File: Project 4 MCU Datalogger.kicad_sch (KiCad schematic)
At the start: 0 parts

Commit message: Setup of EEschema of new project.
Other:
- company: (none) -> Mad Tech T
- title: (none) -> ${project_name}
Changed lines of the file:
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@@
 	(generator_version "9.0")
 	(paper "A4")
+	(title_block
+		(title "${project_name}")
+		(date "2025-11-02")
+		(rev "1")
+		(company "Mad Tech T")
+	)
 	(sheet_instances
 		(path "/"

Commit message: Added required symbols to the schematic sheet.
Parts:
- added BT1: Battery, symbol Device:Battery
- added C1, C2, C4, C5: C, symbol Device:C
- added C3: C_Polarized, symbol Device:C_Polarized
- added D1, D2: LED, symbol Device:LED
- added H1, H2, H3, H4: MountingHole, symbol Mechanical:MountingHole
- added R1, R2, R3, R4, R5, R6, R7: R, symbol Device:R
- added U1, U2: 24LC1025, symbol Memory_EEPROM:24LC1025
- added U3: DS1337S_, DS1337S_:SOIC127P600X175-8N, symbol DS1337S_:DS1337S_
- added U4: ATMEGA328P-AU, ATMEGA328P-AU:QFP80P900X900X120-32N, symbol ATMEGA328P-AU:ATMEGA328P-AU
- added Y1, Y2: Crystal, symbol Device:Crystal
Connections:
- new net: U3.1 (X1), Y1.2
- new net: U3.2 (X2), Y1.1
- new net: R5.2, U3.3 (~{INTA})
- new net: R6.2, U3.7 (SQW/~INT)
- new net: C5.1, R5.1, R6.1, U3.8 (VCC)
- new net: D1.1 (K), R4.2
- new net: D1.2 (A), U4.17 (PB5)
- new net: BT1.1 (+), C3.1, D2.2 (A), U4.18 (AVCC)
- new net: D2.1 (K), R1.1
- new net: R2.1, R3.1
- new net: C1.2, U4.7 (PB6), Y2.2
- new net: R7.2, U4.29 (PC6/~{RESET})
- new net: C2.2, U4.8 (PB7), Y2.1
- new net: C4.2, U4.12 (PB0)
- new net: U4.21 (GND), U4.3 (GND), U4.5 (GND)
- new net: U4.4 (VCC), U4.6 (VCC)
- new net GND: BT1.2 (-), C1.1, C2.1, C3.2, C4.1, C5.2, R1.2, R4.1, U1.4 (GND), U1.7 (WP), U2.2 (A1), U2.4 (GND), U2.7 (WP), U3.4 (GND)
- no-connect marks 0 -> 8
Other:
- added sheet Connectors (connectors.kicad_sch)

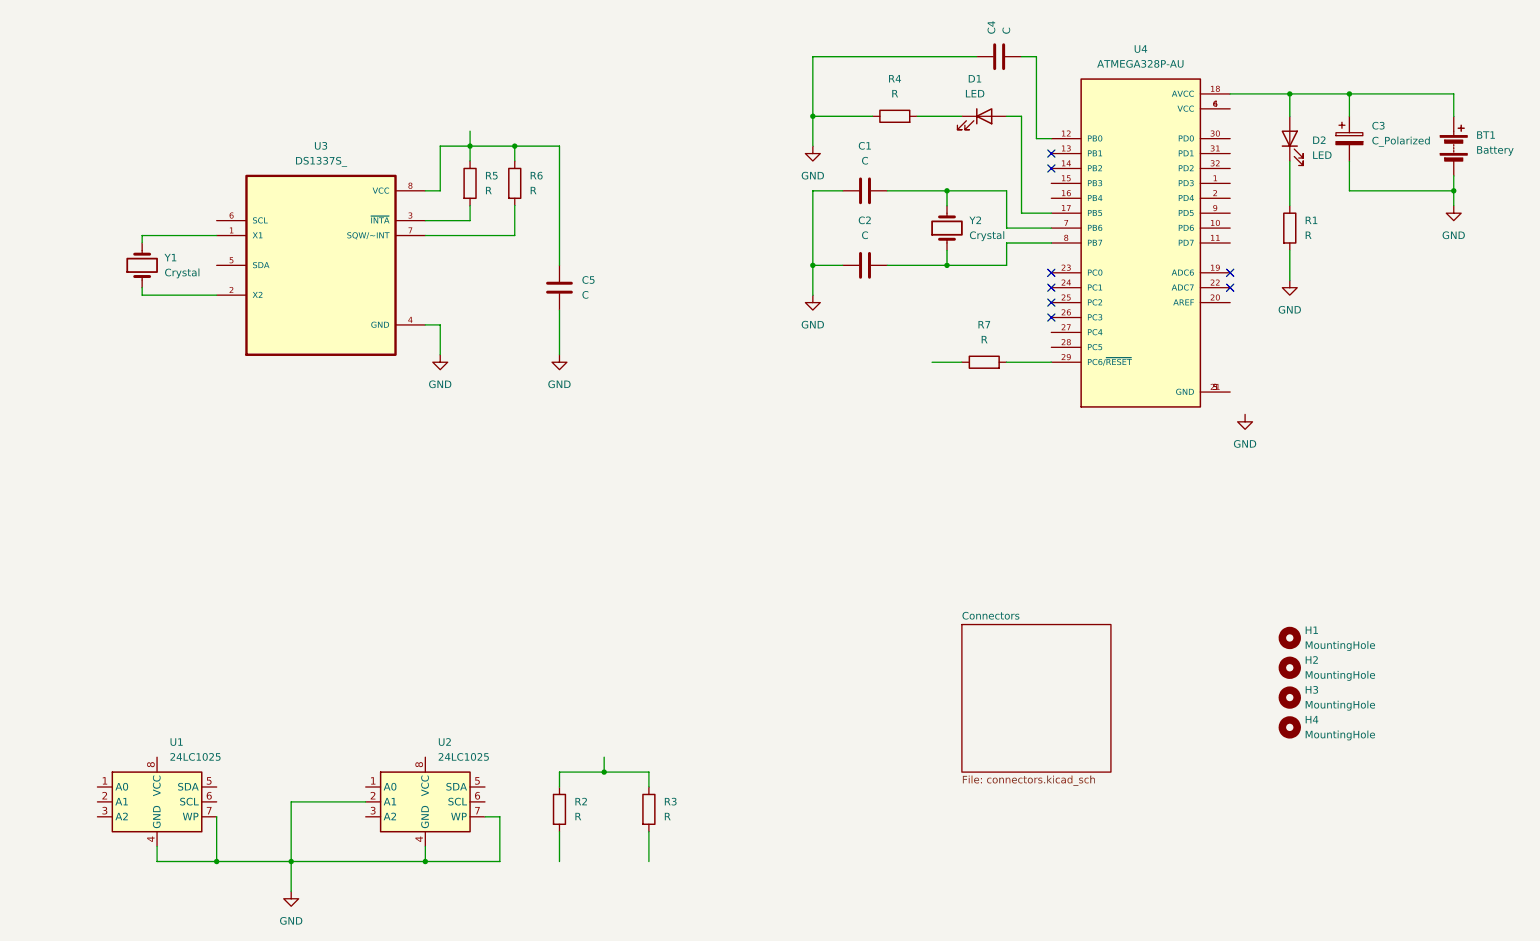
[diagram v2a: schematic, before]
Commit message: completed symbol-footprint association.
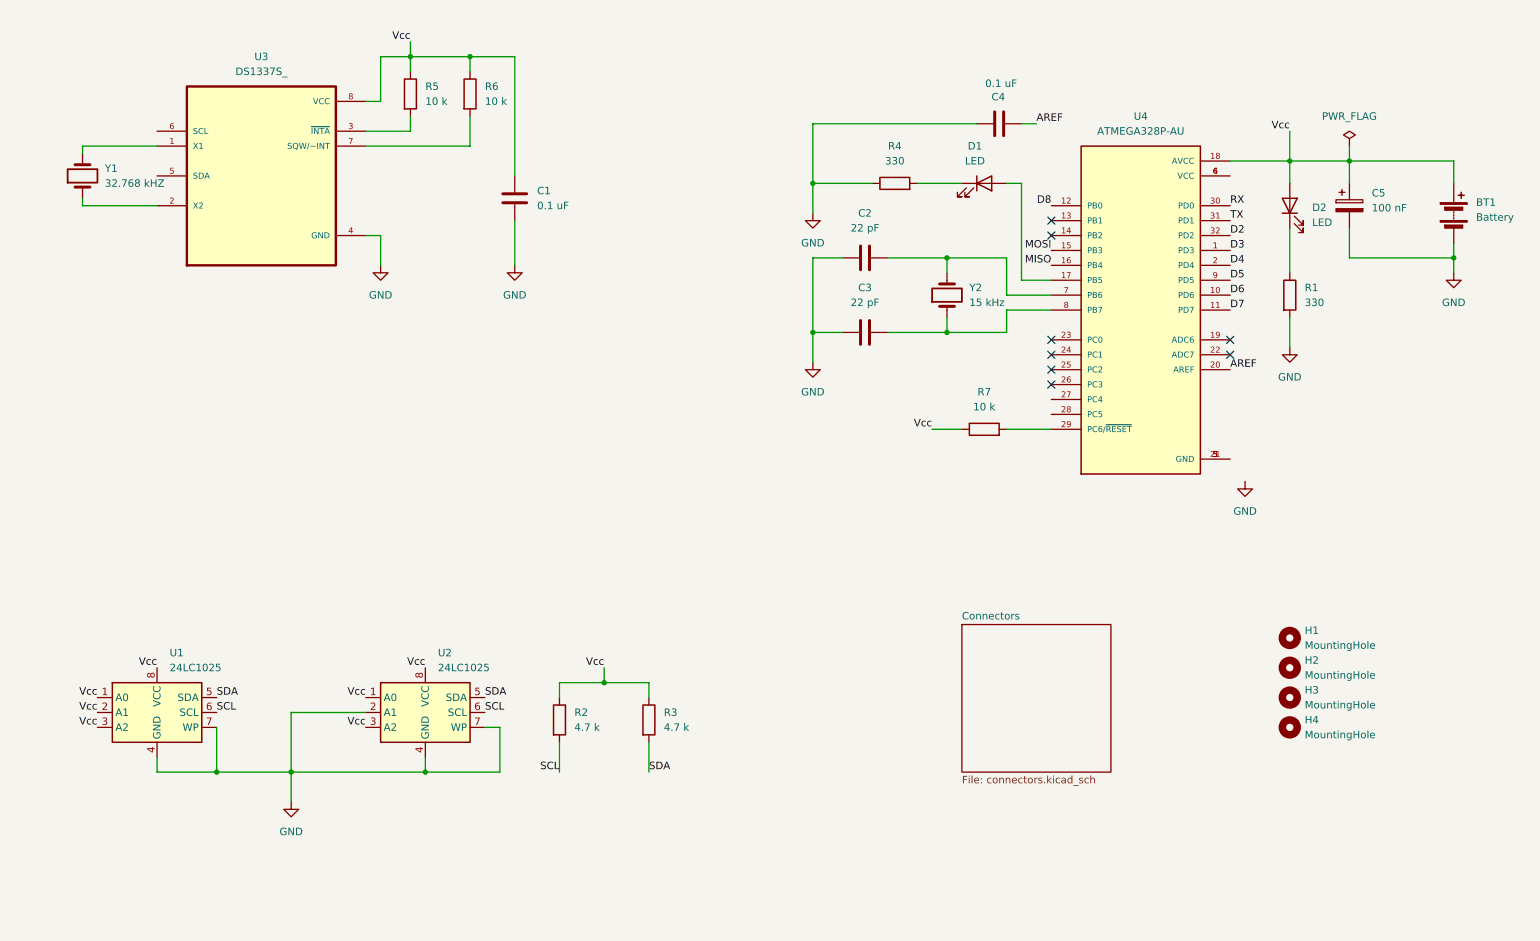
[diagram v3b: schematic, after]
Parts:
- BT1: footprint (none) -> Connector_PinHeader_2.54mm:PinHeader_1x02_P2.54mm_Vertical
- C1: renamed from C5; value C -> 0.1 uF; footprint (none) -> Capacitor_SMD:C_0805_2012Metric
- C2: renamed from C1; value C -> 22 pF; footprint (none) -> Capacitor_SMD:C_0805_2012Metric
- C3: renamed from C2; value C -> 22 pF; footprint (none) -> Capacitor_SMD:C_0805_2012Metric
- C4: value C -> 0.1 uF; footprint (none) -> Capacitor_SMD:C_0805_2012Metric
- C5: renamed from C3; value C_Polarized -> 100 nF; footprint (none) -> Capacitor_SMD:C_0805_2012Metric
- D1, D2: footprint (none) -> LED_SMD:LED_0805_2012Metric
- H1, H2, H3, H4: footprint (none) -> MountingHole:MountingHole_2.1mm
- R1, R4: value R -> 330; footprint (none) -> Resistor_SMD:R_0805_2012Metric
- R2, R3: value R -> 4.7 k; footprint (none) -> Resistor_SMD:R_0805_2012Metric
- R5, R6, R7: value R -> 10 k; footprint (none) -> Resistor_SMD:R_0805_2012Metric
- U1, U2: footprint (none) -> Package_SO:SOIC-8_5.3x5.3mm_P1.27mm
- U3: footprint DS1337S_:SOIC127P600X175-8N -> MCU_Datalogger_Footprints:SOIC127P600X175-8N
- U4: footprint ATMEGA328P-AU:QFP80P900X900X120-32N -> MCU_Datalogger_Footprints:QFP80P900X900X120-32N
- Y1: value Crystal -> 32.768 kHZ; footprint (none) -> Crystal:Crystal_SMD_5032-2Pin_5.0x3.2mm
- Y2: value Crystal -> 15 kHz; footprint (none) -> Crystal:Crystal_SMD_5032-2Pin_5.0x3.2mm
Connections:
- net Vcc: now reaches C1.1, R5.1, R6.1, U3.8 (VCC)
- net Vcc: now also BT1.1 (+), C5.1, D2.2 (A), R2.1, R3.1, R7.1, U1.1 (A0), U1.2 (A1), U1.3 (A2), U1.8 (VCC), U2.1 (A0), U2.3 (A2), U2.8 (VCC), U4.18 (AVCC)
- net SCL: now reaches R2.2
- net SCL: now also U1.6 (SCL), U2.6 (SCL)
- net SDA: now reaches U2.5 (SDA)
- net SDA: now also R3.2, U1.5 (SDA)
- net AREF: now reaches C4.2
- net AREF: now also U4.20 (AREF); no longer U4.12 (PB0)
- net D3: now reaches U4.1 (PD3)
- net D6: now reaches U4.10 (PD6)
- net D7: now reaches U4.11 (PD7)
- net MOSI: now reaches U4.15 (PB3)
- net MISO: now reaches U4.16 (PB4)
- net D4: now reaches U4.2 (PD4)
- net RX: now reaches U4.30 (PD0)
- net TX: now reaches U4.31 (PD1)
- net D2: now reaches U4.32 (PD2)
- net D5: now reaches U4.9 (PD5)
- new net D8: U4.12 (PB0)
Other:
- moved on the sheet: BT1, C1, C2, C3, C4, C5, D1, D2, R1, R2, R3, R4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

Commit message: Completed wiring in the second sheet.
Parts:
- C1, C4: value 0.1 uF -> 0.1uF
- C2, C3: value 22 pF -> 22pF
- C5: value 100 nF -> 100nF
- R2, R3: value 4.7 k -> 4.7k
- R5, R6, R7: value 10 k -> 10k
- Y1: value 32.768 kHZ -> 32.768kHZ
- Y2: value 15 kHz -> 16MHz
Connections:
- net GND: now also U4.21 (GND), U4.3 (GND), U4.5 (GND)
- net SCL: now also U3.6 (SCL), U4.28 (PC5)
- net SDA: now also U3.5 (SDA), U4.27 (PC4)
- net Vcc: now also U4.4 (VCC)
- net SCK: now reaches D1.2 (A), U4.17 (PB5)
- net RESET: now reaches R7.2, U4.29 (PC6/~{RESET})
- net at U4.6 (VCC): no longer U4.4 (VCC)
- net AREF: no longer names the net of C4.2, U4.20 (AREF)
- no-connect marks 8 -> 9
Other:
- sheet Connectors ports: added D2, D3, D4, D5, D6, D7, D8, GND, MISO, MOSI, RESET, RX, SCK, SCL, SDA, TX, Vcc; removed none
- moved on the sheet: C4, H2, H3, H4, Y1

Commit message: Completed Comments.
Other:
- note added: "EEPROM"
- note added: "MCU"
- note added: "Mounting Holes"
- note added: "Real Time Clock"
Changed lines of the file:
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@@
 		(company "Mad Tech T")
+	)
+	(text "MCU"
+		(exclude_from_sim no)
+		(at 149.098 32.004 0)
+		(effects
+			(font
+				(size 1.27 1.27)
+			)
+		)
+	)
+	(text "EEPROM"
+		(exclude_from_sim no)
+		(at 29.21 125.984 0)
+		(effects
+			(font
+				(size 1.27 1.27)
+			)
+		)
+	)
+	(text "Mounting Holes"
+		(exclude_from_sim no)
+		(at 235.966 123.444 0)
+		(effects
+			(font
+				(size 1.27 1.27)
+			)
+		)
+	)
+	(text "Real Time Clock"
+		(exclude_from_sim no)
+		(at 25.4 24.384 0)
+		(effects
+			(font
+				(size 1.27 1.27)
+			)
+		)
 	)
 	(junction
@@
 		)
 	)
+	(polyline
+		(pts
+			(xy 228.6 157.48) (xy 254 157.48)
+		)
+		(stroke
+			(width 0)
+			(type default)
+		)
+	)
 	(wire
 		(pts
@@
 		)
 	)
+	(polyline
+		(pts
+			(xy 17.78 25.4) (xy 18.288 25.4)
+		)
+		(stroke
+			(width 0)
+			(type default)
+		)
+	)
 	(wire
 		(pts
@@
 		)
 	)
+	(polyline
+		(pts
+			(xy 17.78 76.2) (xy 17.78 25.4)
+		)
+		(stroke
+			(width 0)
+			(type default)
+		)
+	)
 	(wire
 		(pts
@@
 		)
 	)
+	(polyline
+		(pts
+			(xy 25.4 165.1) (xy 131.826 165.1)
+		)
+		(stroke
+			(width 0)
+			(type default)
+		)
+	)
 	(wire
 		(pts
@@
 		)
 	)
+	(polyline
+		(pts
+			(xy 25.4 127) (xy 25.4 165.1)
+		)
+		(stroke
+			(width 0)
+			(type default)
+		)
+	)
 	(wire
 		(pts
@@
 		)
 	)
+	(polyline
+		(pts
+			(xy 274.32 111.76) (xy 147.32 111.76)
+		)
+		(stroke
+			(width 0)
+			(type default)
+		)
+	)
 	(wire
 		(pts
@@
 		)
 	)
+	(polyline
+		(pts
+			(xy 147.32 111.76) (xy 147.32 33.02)
+		)
+		(stroke
+			(width 0)
+			(type default)
+		)
+	)
 	(wire
 		(pts
@@
 		)
 	)
+	(polyline
+		(pts
+			(xy 274.32 33.02) (xy 274.32 111.76)
+		)
+		(stroke
+			(width 0)
+			(type default)
+		)
+	)
 	(wire
 		(pts
@@
 		)
 	)
+	(polyline
+		(pts
+			(xy 254 124.46) (xy 228.6 124.46)
+		)
+		(stroke
+			(width 0)
+			(type default)
+		)
+	)
 	(wire
 		(pts
@@
 		)
 	)
+	(polyline
+		(pts
+			(xy 25.4 127) (xy 131.826 127)
+		)
+		(stroke
+			(width 0)
+			(type default)
+		)
+	)
 	(wire
 		(pts
@@
 		)
 	)
+	(polyline
+		(pts
+			(xy 111.76 76.2) (xy 17.78 76.2)
+		)
+		(stroke
+			(width 0)
+			(type default)
+		)
+	)
+	(polyline
+		(pts
+			(xy 111.76 25.4) (xy 111.76 76.2)
+		)
+		(stroke
+			(width 0)
+			(type default)
+		)
+	)
 	(wire
 		(pts
@@
 		)
 	)
+	(polyline
+		(pts
+			(xy 17.78 25.4) (xy 111.76 25.4)
+		)
+		(stroke
+			(width 0)
+			(type default)
+		)
+	)
+	(polyline
+		(pts
+			(xy 131.826 165.1) (xy 131.826 127)
+		)
+		(stroke
+			(width 0)
+			(type default)
+		)
+	)
 	(wire
 		(pts
@@
 		)
 	)
+	(polyline
+		(pts
+			(xy 147.32 33.02) (xy 147.828 33.02)
+		)
+		(stroke
+			(width 0)
+			(type default)
+		)
+	)
 	(wire
 		(pts
@@
 		)
 	)
+	(polyline
+		(pts
+			(xy 254 157.48) (xy 254 124.46)
+		)
+		(stroke
+			(width 0)
+			(type default)
+		)
+	)
 	(wire
 		(pts
@@
 		)
 	)
+	(polyline
+		(pts
+			(xy 228.6 124.46) (xy 228.6 157.48)
+		)
+		(stroke
+			(width 0)
+			(type default)
+		)
+	)
 	(wire
 		(pts
@@
 		)
 		(stroke
+			(width 0)
+			(type default)
+		)
+	)
+	(polyline
+		(pts
+			(xy 147.32 33.02) (xy 274.32 33.02)
+		)
+		(stroke
